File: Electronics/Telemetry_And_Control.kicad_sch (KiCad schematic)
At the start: 31 parts, among them J1 Micro_SD_Card_Det_Hirose_DM3AT, SW10 SW_Push, SW11 SW_Push, SW12 SW_Push, SW13 SW_Push, SW14 SW_Push, SW15 SW_Push, SW6 SW_Push, SW7 ~{USB_BOOT}, SW8 SW_Push, SW9 SW_Push, U5 ESP32-S3-WROOM-1

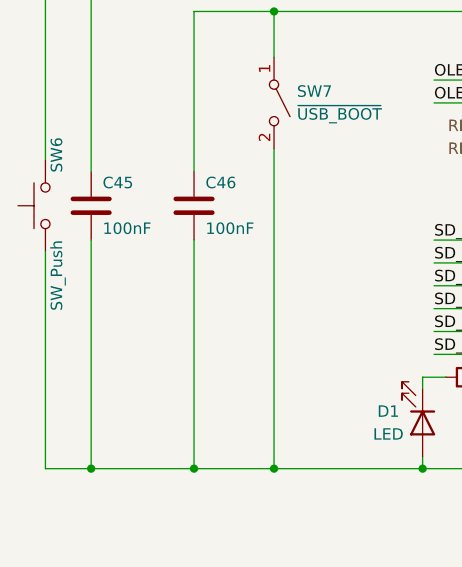
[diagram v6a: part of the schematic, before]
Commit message: started pcb, need bigger frame
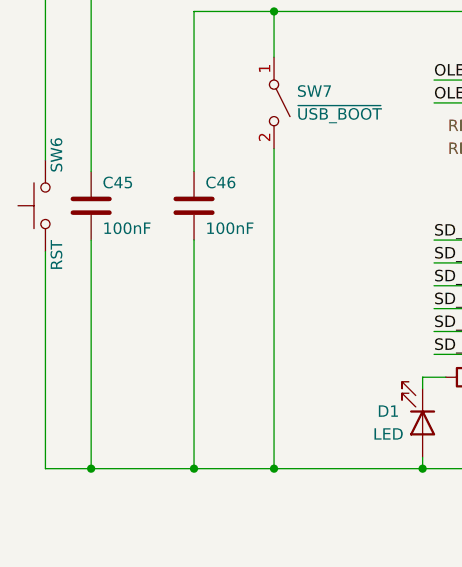
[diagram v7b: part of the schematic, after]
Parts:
- SW10, SW11, SW12, SW13, SW14, SW15, SW8, SW9: footprint Button_Switch_SMD:SW_SPST_TL3342 -> Button_Switch_Keyboard:SW_Cherry_MX_1.00u_PCB
- SW6: value SW_Push -> RST
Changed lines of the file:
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@@
       (effects (font (size 1.27 1.27)))
     )
-    (property "Footprint" "Button_Switch_SMD:SW_SPST_TL3342" (at 63.5 123.19 0)
+    (property "Footprint" "Button_Switch_Keyboard:SW_Cherry_MX_1.00u_PCB" (at 63.5 123.19 0)
       (effects (font (size 1.27 1.27)) hide)
     )
@@
       (effects (font (size 1.27 1.27)))
     )
-    (property "Footprint" "Button_Switch_SMD:SW_SPST_TL3342" (at 63.5 138.43 0)
+    (property "Footprint" "Button_Switch_Keyboard:SW_Cherry_MX_1.00u_PCB" (at 63.5 138.43 0)
       (effects (font (size 1.27 1.27)) hide)
     )
@@
       (effects (font (size 1.27 1.27)))
     )
-    (property "Footprint" "Button_Switch_SMD:SW_SPST_TL3342" (at 63.5 158.75 0)
+    (property "Footprint" "Button_Switch_Keyboard:SW_Cherry_MX_1.00u_PCB" (at 63.5 158.75 0)
       (effects (font (size 1.27 1.27)) hide)
     )
@@
       (effects (font (size 1.27 1.27)))
     )
-    (property "Footprint" "Button_Switch_SMD:SW_SPST_TL3342" (at 63.5 143.51 0)
+    (property "Footprint" "Button_Switch_Keyboard:SW_Cherry_MX_1.00u_PCB" (at 63.5 143.51 0)
       (effects (font (size 1.27 1.27)) hide)
     )
@@
       (effects (font (size 1.27 1.27)))
     )
-    (property "Footprint" "Button_Switch_SMD:SW_SPST_TL3342" (at 63.5 128.27 0)
+    (property "Footprint" "Button_Switch_Keyboard:SW_Cherry_MX_1.00u_PCB" (at 63.5 128.27 0)
       (effects (font (size 1.27 1.27)) hide)
     )
@@
       (effects (font (size 1.27 1.27)) (justify right))
     )
-    (property "Value" "SW_Push" (at 33.02 80.01 0)
+    (property "Value" "RST" (at 33.02 80.01 0)
       (effects (font (size 1.27 1.27)) (justify right))
     )
@@
       (effects (font (size 1.27 1.27)))
     )
-    (property "Footprint" "Button_Switch_SMD:SW_SPST_TL3342" (at 63.5 133.35 0)
+    (property "Footprint" "Button_Switch_Keyboard:SW_Cherry_MX_1.00u_PCB" (at 63.5 133.35 0)
       (effects (font (size 1.27 1.27)) hide)
     )
@@
       (effects (font (size 1.27 1.27)))
     )
-    (property "Footprint" "Button_Switch_SMD:SW_SPST_TL3342" (at 63.5 148.59 0)
+    (property "Footprint" "Button_Switch_Keyboard:SW_Cherry_MX_1.00u_PCB" (at 63.5 148.59 0)
       (effects (font (size 1.27 1.27)) hide)
     )
@@
       (effects (font (size 1.27 1.27)))
     )
-    (property "Footprint" "Button_Switch_SMD:SW_SPST_TL3342" (at 63.5 153.67 0)
-      (effects (font (size 1.27 1.27)) hide)
-    )
+    (property "Footprint" "Button_Switch_Keyboard:SW_Cherry_MX_1.00u_PCB" (at 63.5 153.67 0)
+      (effects (font (size 1.27 1.27)) hide)
+    )
